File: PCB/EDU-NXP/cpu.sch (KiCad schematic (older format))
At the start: 77 parts, among them J7 ZX62-AB-5PA, P8 Cortex-Debug, P9 FT_NC, SW1 SW_PUSH, U14 TXB0108, U16 LPC4337JBD144, U17 FT2232H, U19 93C46, X1 32.768K, X2 12MHz, X3 12MHz

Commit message: Versión completa del esquemático con todos los componentes ya definidos
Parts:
- SW5: renamed from SW1; value SW_PUSH -> RESET
- renumbered C79 to C11, C81 to C12, C82 to C13, C83 to C14, C84 to C15, C85 to C16, C69 to C17, C86 to C18, C87 to C19, C47 to C20, C48 to C21, C49 to C22, C50 to C23, C51 to C24, C52 to C25, C53 to C26, C54 to C27, C55 to C28, C56 to C29, C57 to C30, C58 to C31, C59 to C32, C60 to C33, C90 to C34, C80 to C35, C77 to C36, C78 to C37, C67 to C38, C68 to C39, C61 to C40, C70 to C41, C71 to C42, C72 to C43, C73 to C44, C74 to C45, C75 to C46, C76 to C47, C62 to C48, FB7 to FB5, FB11 to FB6, FB9 to FB7, J7 to J3, JP15 to JP5, P8 to P3, P9 to P4, R102 to R100, R104 to R101, R103 to R102, R97 to R103, R98 to R104, R84 to R105, R85 to R106, R86 to R107, R87 to R108, R88 to R109, R89 to R110, R96 to R91, R95 to R92, R91 to R93, R92 to R94, R99 to R95, R93 to R96, R100 to R97, R94 to R98, R101 to R99, TR1 to TR2, U16 to U4, U19 to U5, U17 to U6, U14 to U7
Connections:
- net labels removed: USB_PPWR, USB_PWR_FAULT
- no-connect marks 41 -> 43

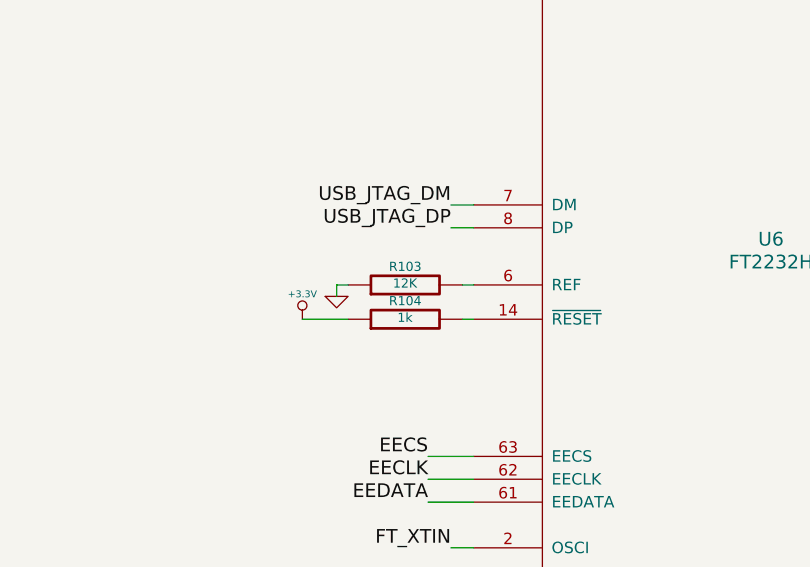
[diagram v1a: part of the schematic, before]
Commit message: El PCB tiene el tamaño de la CIAA-NXP y se colocaron los componentes en una distribución provisoria
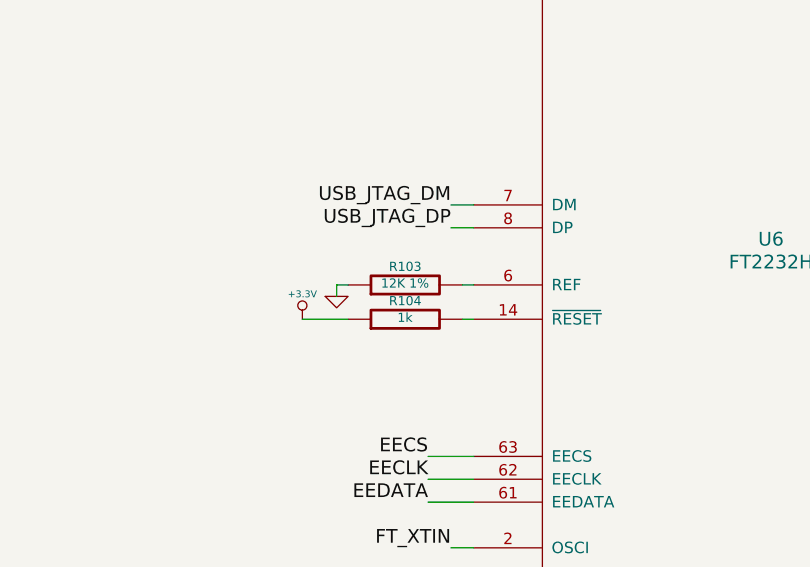
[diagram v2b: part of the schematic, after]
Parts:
- R103: value 12K -> 12K 1%
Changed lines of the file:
@@
 Sheet 7 7
 Title "EDU CIAA CPU - LPC4337"
-Date "24 jun 2014"
+Date "27 jun 2014"
 Rev "1.0"
 Comp ""
@@
 P 10650 7350
 F 0 "R103" V 10730 7350 40  0000 C CNN
-F 1 "12K" V 10657 7351 40  0000 C CNN
+F 1 "12K 1%" V 10657 7351 40  0000 C CNN
 F 2 "~" V 10580 7350 30  0000 C CNN
 F 3 "~" H 10650 7350 30  0000 C CNN

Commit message: Signed-off-by: EFilomena <efilomena@bioingenieria.edu.ar>
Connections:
- wire segments 416 -> 415

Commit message: Se cambiaron los leds - Avances sobre el ruteo del PCB
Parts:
- removed P4: FT_NC, symbol CONN_13X2
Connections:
- net labels added: LED1, LED2, LED3
- net labels removed: LED1_B, LED1_G, LED1_R, LED2_B, LED2_G, LED2_R, LED3_B, LED3_G, LED3_R
- wire segments 415 -> 359
- no-connect marks 43 -> 73

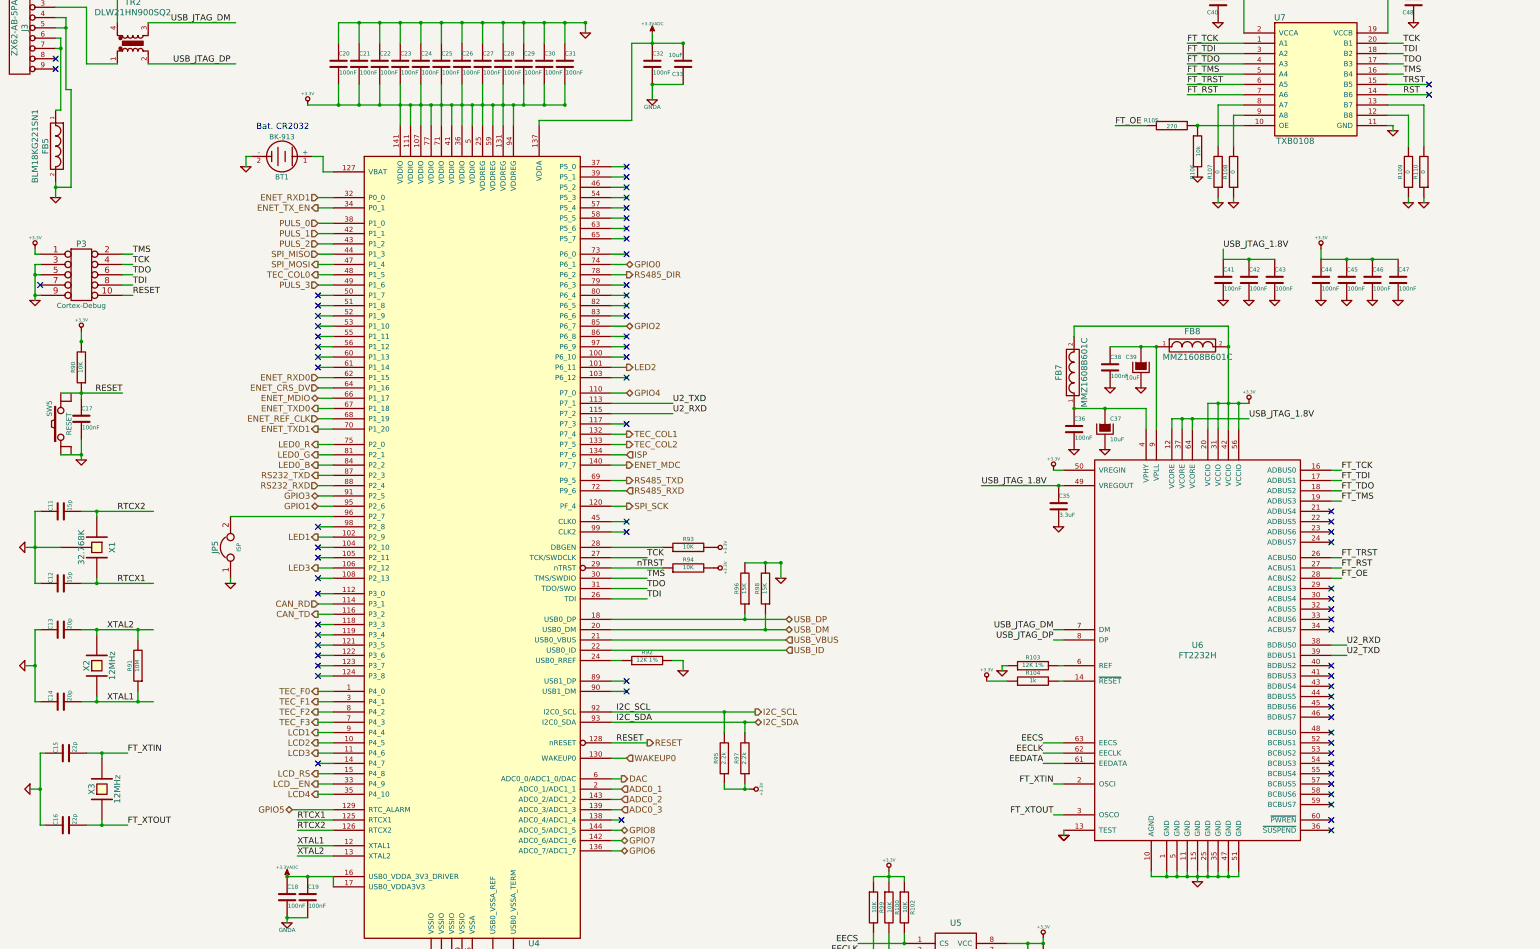
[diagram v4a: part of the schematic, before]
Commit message: Se completó el ruteo del PCB
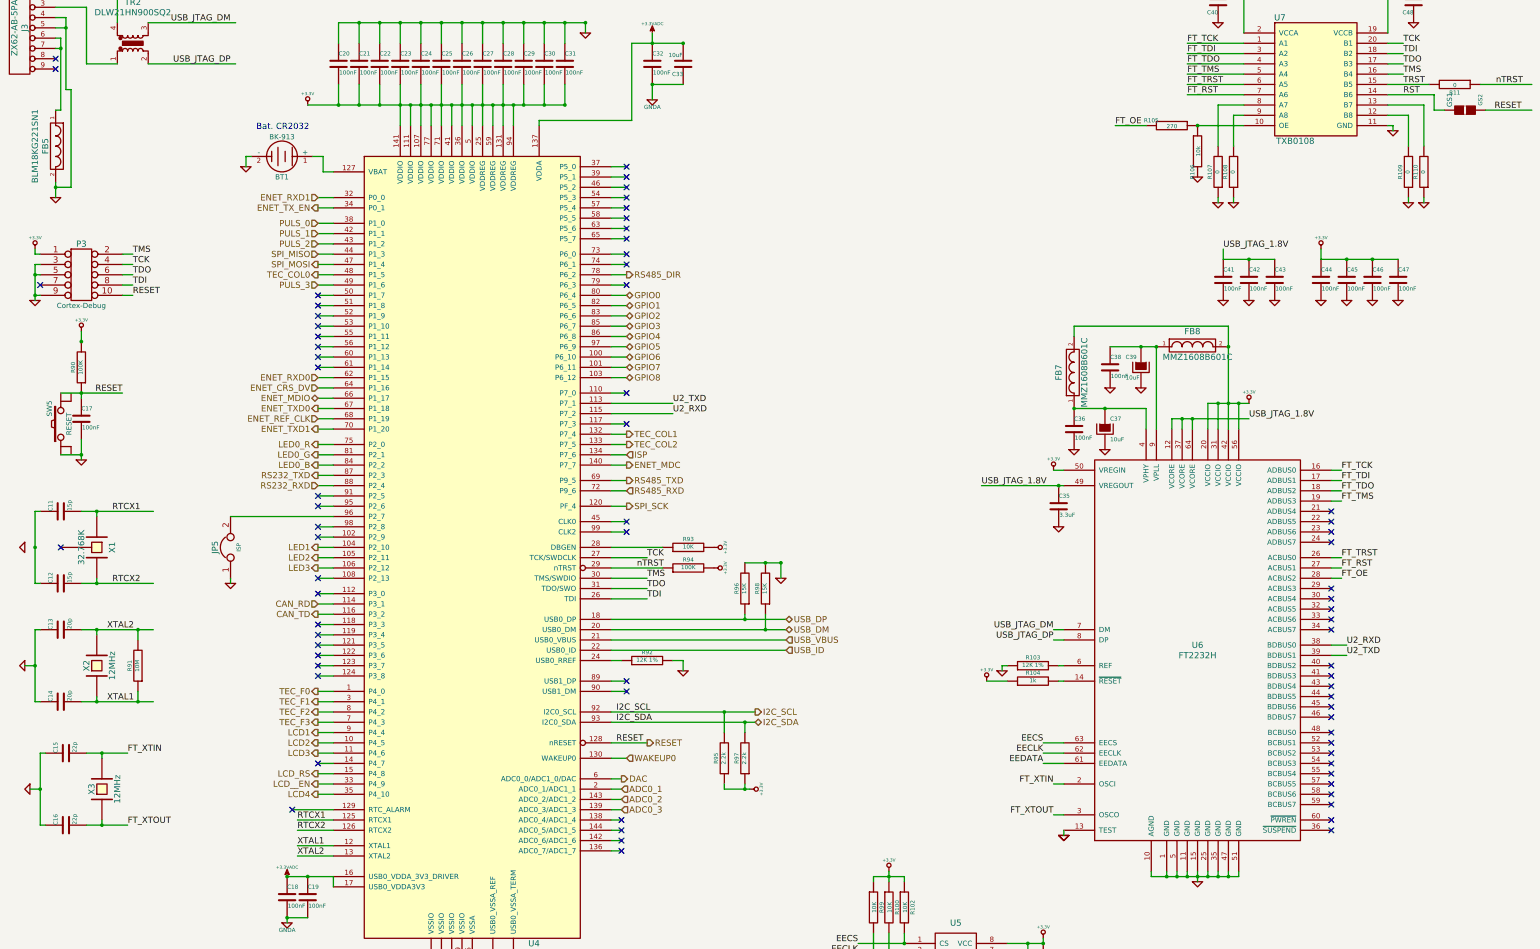
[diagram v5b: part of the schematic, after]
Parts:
- added GS1: GS2, symbol GS2
- added R11: 0, ~, symbol R
- R90, R94: value 10K -> 100K
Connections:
- net GND: no longer C11.1, C12.1, X1.3 (GND)
- net GPIO0: now also U4.80 (P6_4); no longer U4.74 (P6_1)
- net GPIO1: now also U4.82 (P6_5); no longer U4.95 (P2_6)
- net GPIO2: now also U4.83 (P6_6); no longer U4.85 (P6_7)
- net GPIO3: now also U4.85 (P6_7); no longer U4.91 (P2_5)
- net GPIO4: now also U4.86 (P6_8); no longer U4.110 (P7_0)
- net GPIO5: now also U4.97 (P6_9); no longer U4.129 (RTC_ALARM)
- net GPIO6: now also U4.100 (P6_10); no longer U4.136 (ADC0_7/ADC1_7)
- net GPIO7: now also U4.101 (P6_11); no longer U4.142 (ADC0_6/ADC1_6)
- net GPIO8: now also U4.103 (P6_12); no longer U4.144 (ADC0_5/ADC1_5)
- net LED1: now also U4.104 (P2_10); no longer U4.102 (P2_9)
- net LED2: now also U4.105 (P2_11); no longer U4.101 (P6_11)
- net RESET: now also GS1.2 (G2)
- net RST: now also GS1.1 (G1)
- net RTCX1: now also C11.2, X1.1; no longer C12.2, X1.4
- net RTCX2: now also C12.2, X1.4; no longer C11.2, X1.1
- net TRST: now also R11.2
- net nTRST: now also R11.1
- new net: C11.1, C12.1
- no-connect marks 73 -> 72

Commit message: PCB V0.0 finalizado - Se agregaron planos de masa, control de dimensiones y perforaciones, se agregó el LOGO
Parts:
- removed R11: 0, ~, symbol R
- added GS2: GS2, symbol GS2
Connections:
- net GND: now also C11.1, C12.1
- net TRST: now also GS2.1 (G1)
- net nTRST: now also GS2.2 (G2)
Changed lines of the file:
@@
 LIBS:pbss5240xf
 LIBS:LED_RGB
+LIBS:Logo
 LIBS:edu-ciaa-nxp-cache
 EELAYER 27 0
@@
 Sheet 7 7
 Title "EDU CIAA CPU - LPC4337"
-Date "12 jul 2014"
+Date "14 jul 2014"
 Rev "1.0"
 Comp ""
@@
 	14100 1800 14550 1800
 Wire Wire Line
-	14100 1700 14500 1700
+	14100 1700 14600 1700
 Wire Wire Line
 	14100 700  14100 1200
@@
 Text Label 15150 1700 0    60   ~ 0
 nTRST
-$Comp
-L R R11
-U 1 1 53C13AFE
-P 14750 1700
-F 0 "R11" V 14830 1700 40  0000 C CNN
-F 1 "0" V 14757 1701 40  0000 C CNN
-F 2 "~" V 14680 1700 30  0000 C CNN
-F 3 "~" H 14750 1700 30  0000 C CNN
-	1    14750 1700
-	0    1    1    0
-$EndComp
 Wire Wire Line
 	15000 1700 15500 1700
@@
 U 1 1 53C140A7
 P 14850 1950
-F 0 "GS1" H 14950 2100 50  0000 C CNN
-F 1 "GS2" H 14950 1801 40  0000 C CNN
+F 0 "GS1" V 14950 1900 50  0000 C CNN
+F 1 "GS2" H 14950 1801 40  0001 C CNN
 F 2 "" H 14850 1950 60  0000 C CNN
 F 3 "" H 14850 1950 60  0000 C CNN
@@
 	15050 1950 15500 1950
 NoConn ~ 1200 6200
+Wire Wire Line
+	950  6200 850  6200
+$Comp
+L LOGO #G7
+U 1 1 53C3FC6C
+P 15400 10000
+F 0 "#G7" H 15400 9597 60  0001 C CNN
+F 1 "LOGO" H 15400 10403 60  0001 C CNN
+F 2 "" H 15400 10000 60  0000 C CNN
+F 3 "" H 15400 10000 60  0000 C CNN
+	1    15400 10000
+	1    0    0    -1
+$EndComp
+$Comp
+L GS2 GS2
+U 1 1 53C3DD6E
+P 14800 1700
+F 0 "GS2" V 14900 1650 50  0000 C CNN
+F 1 "GS2" H 14900 1551 40  0001 C CNN
+F 2 "" H 14800 1700 60  0000 C CNN
+F 3 "" H 14800 1700 60  0000 C CNN
+	1    14800 1700
+	0    -1   -1   0
+$EndComp
 $EndSCHEMATC

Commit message: Teclas THT y conectores micro USB THT
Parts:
- removed GS1, GS2: GS2, symbol GS2
- added R11, R15: 0, ~, symbol R
- J3: value ZX62-AB-5PA -> ZX62-AB-5P8
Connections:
- net GND: now also SW5.3, SW5.4; no longer SW5.1
- net RESET: now also SW5.1, SW5.2, R15.1; no longer SW5.3
- net RST: now also R15.2
- net TRST: now also R11.2
- net nTRST: now also R11.1
- net CHJ3: now reaches FB5.1, J3.6 (P6), J3.7 (P7)
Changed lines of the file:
@@
 LIBS:LED_RGB
 LIBS:Logo
+LIBS:edu-ciaa-logo
 LIBS:edu-ciaa-nxp-cache
 EELAYER 27 0
@@
 Sheet 7 7
 Title "EDU CIAA CPU - LPC4337"
-Date "14 jul 2014"
+Date "17 jul 2014"
 Rev "1.0"
 Comp ""
@@
 F 3 "~" H 1200 5000 60  0000 C CNN
 	1    1200 5000
-	0    -1   -1   0
+	0    -1   1    0
 $EndComp
 $Comp
@@
 P 800 1150
 F 0 "J3" V 750 1150 60  0000 C CNN
-F 1 "ZX62-AB-5PA" V 850 1150 60  0000 C CNN
+F 1 "ZX62-AB-5P8" V 850 1150 60  0000 C CNN
 F 2 "" H 800 1150 60  0000 C CNN
 F 3 "" H 800 1150 60  0000 C CNN
@@
 Text HLabel 6700 4550 2    60   BiDi ~ 0
 GPIO8
-Text Label 15150 1700 0    60   ~ 0
+Text Label 15250 1700 0    60   ~ 0
 nTRST
 Wire Wire Line
-	15000 1700 15500 1700
-Text Label 15400 1950 2    60   ~ 0
+	15100 1700 15600 1700
+Text Label 15500 1950 2    60   ~ 0
 RESET
 Wire Wire Line
@@
 Wire Wire Line
 	14550 1950 14650 1950
-$Comp
-L GS2 GS1
-U 1 1 53C140A7
-P 14850 1950
-F 0 "GS1" V 14950 1900 50  0000 C CNN
-F 1 "GS2" H 14950 1801 40  0001 C CNN
-F 2 "" H 14850 1950 60  0000 C CNN
-F 3 "" H 14850 1950 60  0000 C CNN
-	1    14850 1950
-	0    -1   -1   0
-$EndComp
-Wire Wire Line
-	15050 1950 15500 1950
+Wire Wire Line
+	15150 1950 15600 1950
 NoConn ~ 1200 6200
 Wire Wire Line
@@
 $EndComp
 $Comp
-L GS2 GS2
-U 1 1 53C3DD6E
-P 14800 1700
-F 0 "GS2" V 14900 1650 50  0000 C CNN
-F 1 "GS2" H 14900 1551 40  0001 C CNN
-F 2 "" H 14800 1700 60  0000 C CNN
-F 3 "" H 14800 1700 60  0000 C CNN
-	1    14800 1700
-	0    -1   -1   0
-$EndComp
+L R R11
+U 1 1 53C44596
+P 14850 1700
+F 0 "R11" V 14930 1700 40  0000 C CNN
+F 1 "0" V 14857 1701 40  0000 C CNN
+F 2 "~" V 14780 1700 30  0000 C CNN
+F 3 "~" H 14850 1700 30  0000 C CNN
+	1    14850 1700
+	0    1    1    0
+$EndComp
+$Comp
+L R R15
+U 1 1 53C4459C
+P 14900 1950
+F 0 "R15" V 14980 1950 40  0000 C CNN
+F 1 "0" V 14907 1951 40  0000 C CNN
+F 2 "~" V 14830 1950 30  0000 C CNN
+F 3 "~" H 14900 1950 30  0000 C CNN
+	1    14900 1950
+	0    1    1    0
+$EndComp
+Connection ~ 1300 4700
+Connection ~ 1300 5300
+Text Label 950  1850 0    60   ~ 0
+CHJ3
+Wire Wire Line
+	1200 1850 950  1850
+Connection ~ 1200 1850
 $EndSCHEMATC

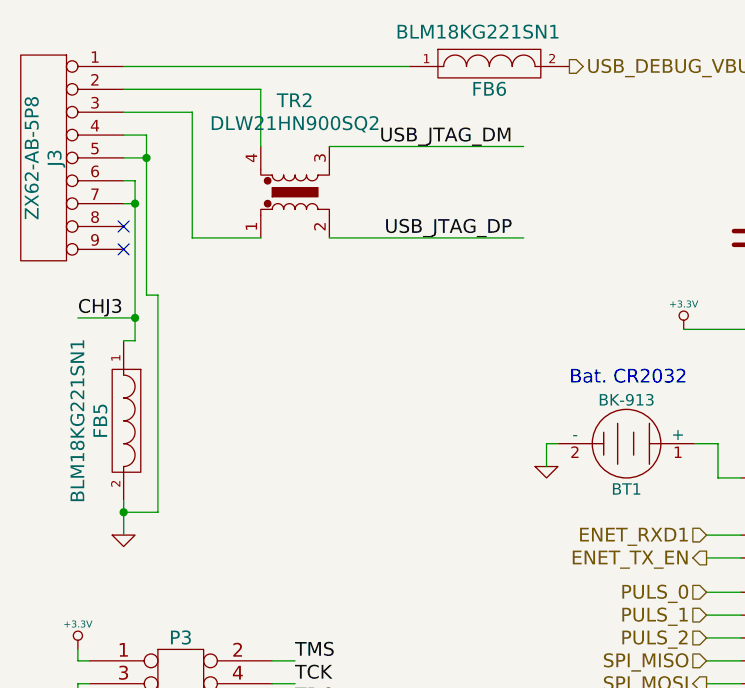
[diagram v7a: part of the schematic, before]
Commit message: Cambio de filtros en 0603 por MI0805M221R-10 (encapsulado 0805)
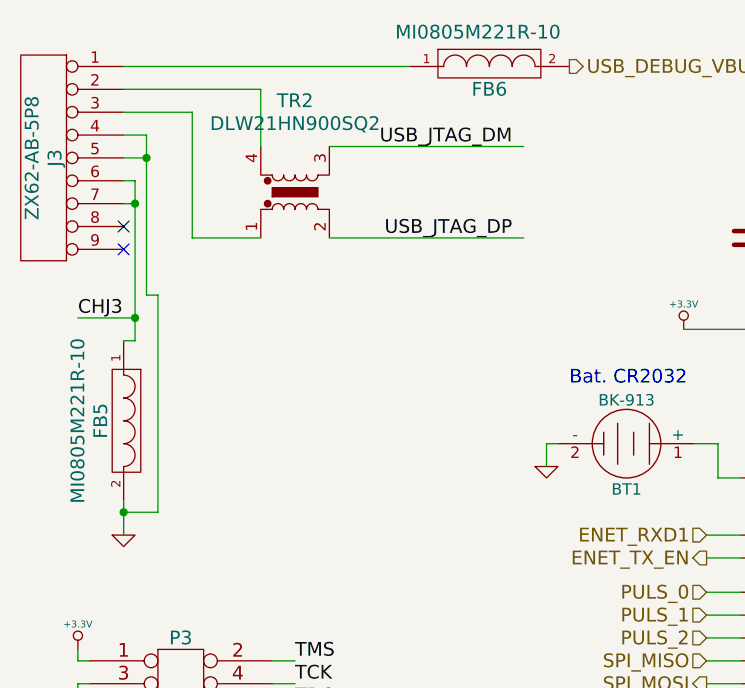
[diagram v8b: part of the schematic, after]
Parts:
- FB5, FB6: value BLM18KG221SN1 -> MI0805M221R-10
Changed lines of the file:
@@
 Sheet 7 7
 Title "EDU CIAA CPU - LPC4337"
-Date "17 jul 2014"
+Date "23 jul 2014"
 Rev "1.0"
 Comp ""
@@
 P 2750 750
 F 0 "FB6" H 2750 650 60  0000 C CNN
-F 1 "BLM18KG221SN1" H 2700 900 60  0000 C CNN
+F 1 "MI0805M221R-10" H 2700 900 60  0000 C CNN
 F 2 "~" H 2750 750 60  0000 C CNN
 F 3 "~" H 2750 750 60  0000 C CNN
@@
 P 1150 2300
 F 0 "FB5" H 1150 2200 60  0000 C CNN
-F 1 "BLM18KG221SN1" H 1150 2100 60  0000 C CNN
+F 1 "MI0805M221R-10" H 1150 2100 60  0000 C CNN
 F 2 "~" H 1150 2300 60  0000 C CNN
 F 3 "~" H 1150 2300 60  0000 C CNN
